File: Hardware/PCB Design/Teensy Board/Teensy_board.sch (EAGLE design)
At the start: 37 parts, among them IC1 MC7805BDTRKG, IC2 UA78M33CKVU, Q1 PROGRAM_FET, U1 PCA9685PW, U2 74HC4051PW,118, U3 74HC4051PW,118, X8 UART

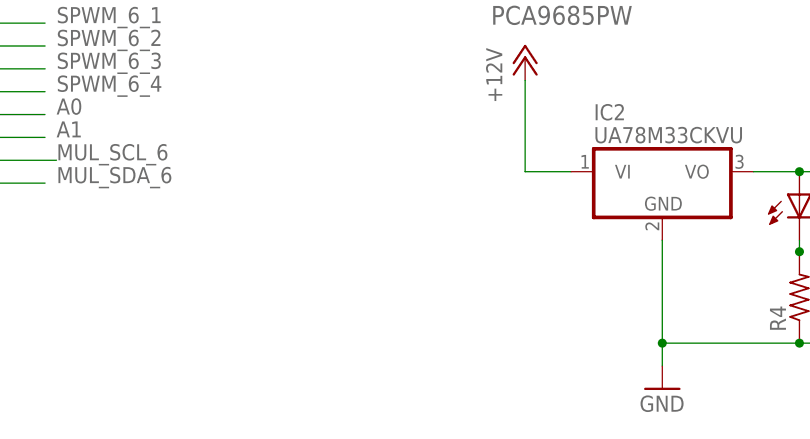
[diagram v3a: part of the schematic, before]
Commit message: Updated signal LEDS
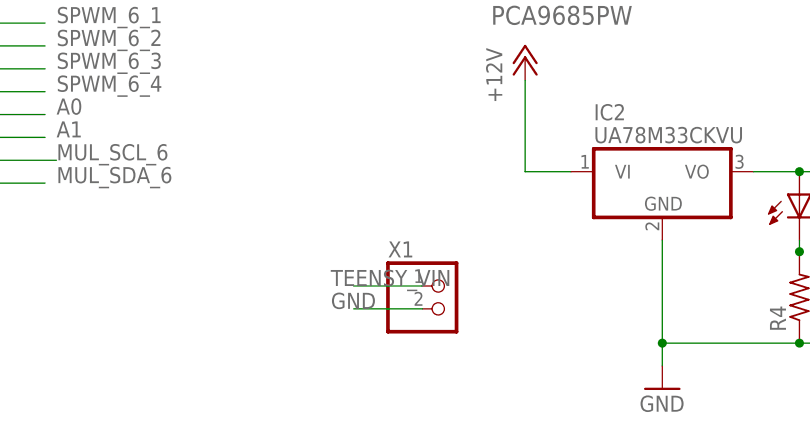
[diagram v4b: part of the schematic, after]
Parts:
- added X1: (no value), CBLA_Test_bed_Library:PINHD-1X2
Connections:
- net GND: now also X1.2
- net TEENSY_VIN: now also X1.1
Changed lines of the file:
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@@
 <?xml version="1.0" encoding="utf-8"?>
 <!DOCTYPE eagle SYSTEM "eagle.dtd">
-<eagle version="7.1.0">
+<eagle version="7.0.0">
 <drawing>
 <settings>
@@
 <part name="X7" library="con-wago-508" deviceset="W237-04P" device=""/>
 <part name="X9" library="con-wago-508" deviceset="W237-04P" device=""/>
+<part name="X1" library="CBLA_Test_bed_Library" deviceset="PINHD-1X2" device=""/>
 </parts>
 <sheets>
@@
 <instance part="X9" gate="-3" x="257.81" y="44.45" rot="R90"/>
 <instance part="X9" gate="-4" x="257.81" y="67.31" rot="R270"/>
+<instance part="X1" gate="G$1" x="86.36" y="17.78"/>
 </instances>
 <busses>
@@
 <pinref part="X7" gate="-2" pin="KL"/>
 </segment>
+<segment>
+<pinref part="X1" gate="G$1" pin="2"/>
+<wire x1="83.82" y1="17.78" x2="76.2" y2="17.78" width="0.1524" layer="91"/>
+<label x="73.66" y="17.78" size="1.778" layer="95"/>
+</segment>
 </net>
 <net name="+3V3" class="0">
@@
 <wire x1="189.23" y1="184.15" x2="189.23" y2="158.75" width="0.1524" layer="91"/>
 </segment>
-</net>
+<segment>
+<pinref part="X1" gate="G$1" pin="1"/>
+<wire x1="83.82" y1="20.32" x2="76.2" y2="20.32" width="0.1524" layer="91"/>
+<label x="73.66" y="20.32" size="1.778" layer="95"/>
+</segment>
+</net>
